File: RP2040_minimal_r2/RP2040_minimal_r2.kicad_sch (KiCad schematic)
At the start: 44 parts, among them J1 SPI0.6, J10 B22, J11 B23, J12 Breakout, J2 SPI0.8, J3 SPI1.13, J4 I2C0, J5 USB, J6 B18, J7 B19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

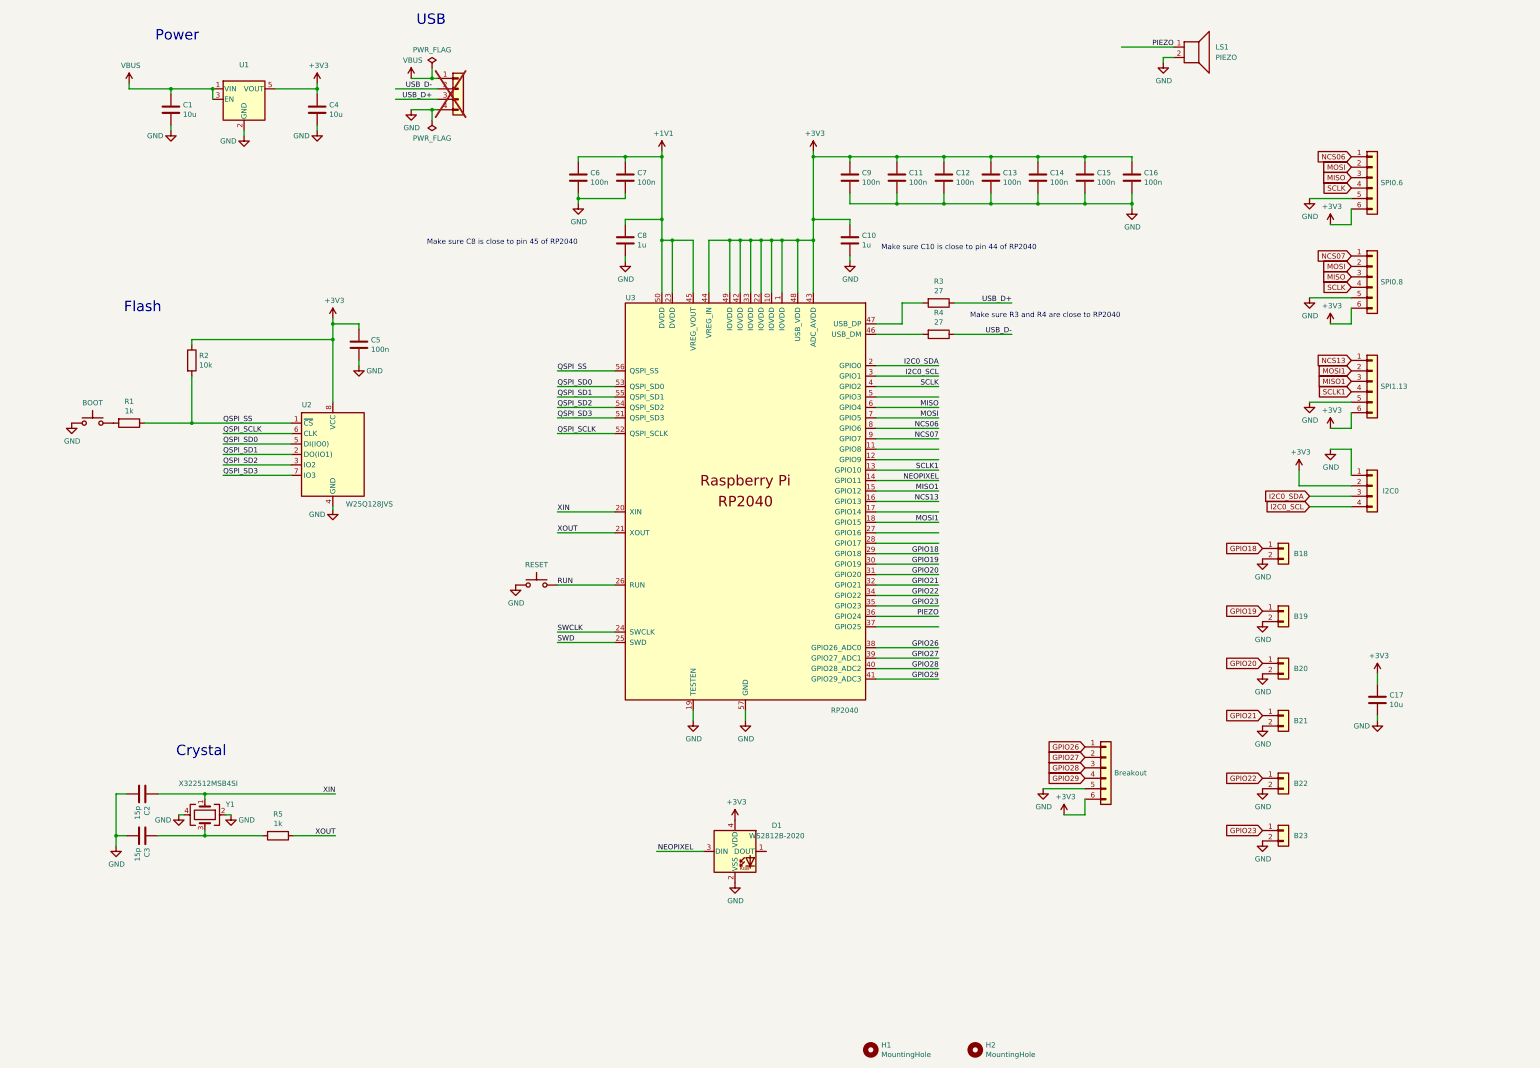
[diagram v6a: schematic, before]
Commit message: Fix incorrect pins used for SPI0. Changed button pins to GPIO 16-21 for slightly cleaner layout. Moved USB header closer to board edge, to allow JST-XH connector to be attached the other way around. Other minor tweaks to top side layout.
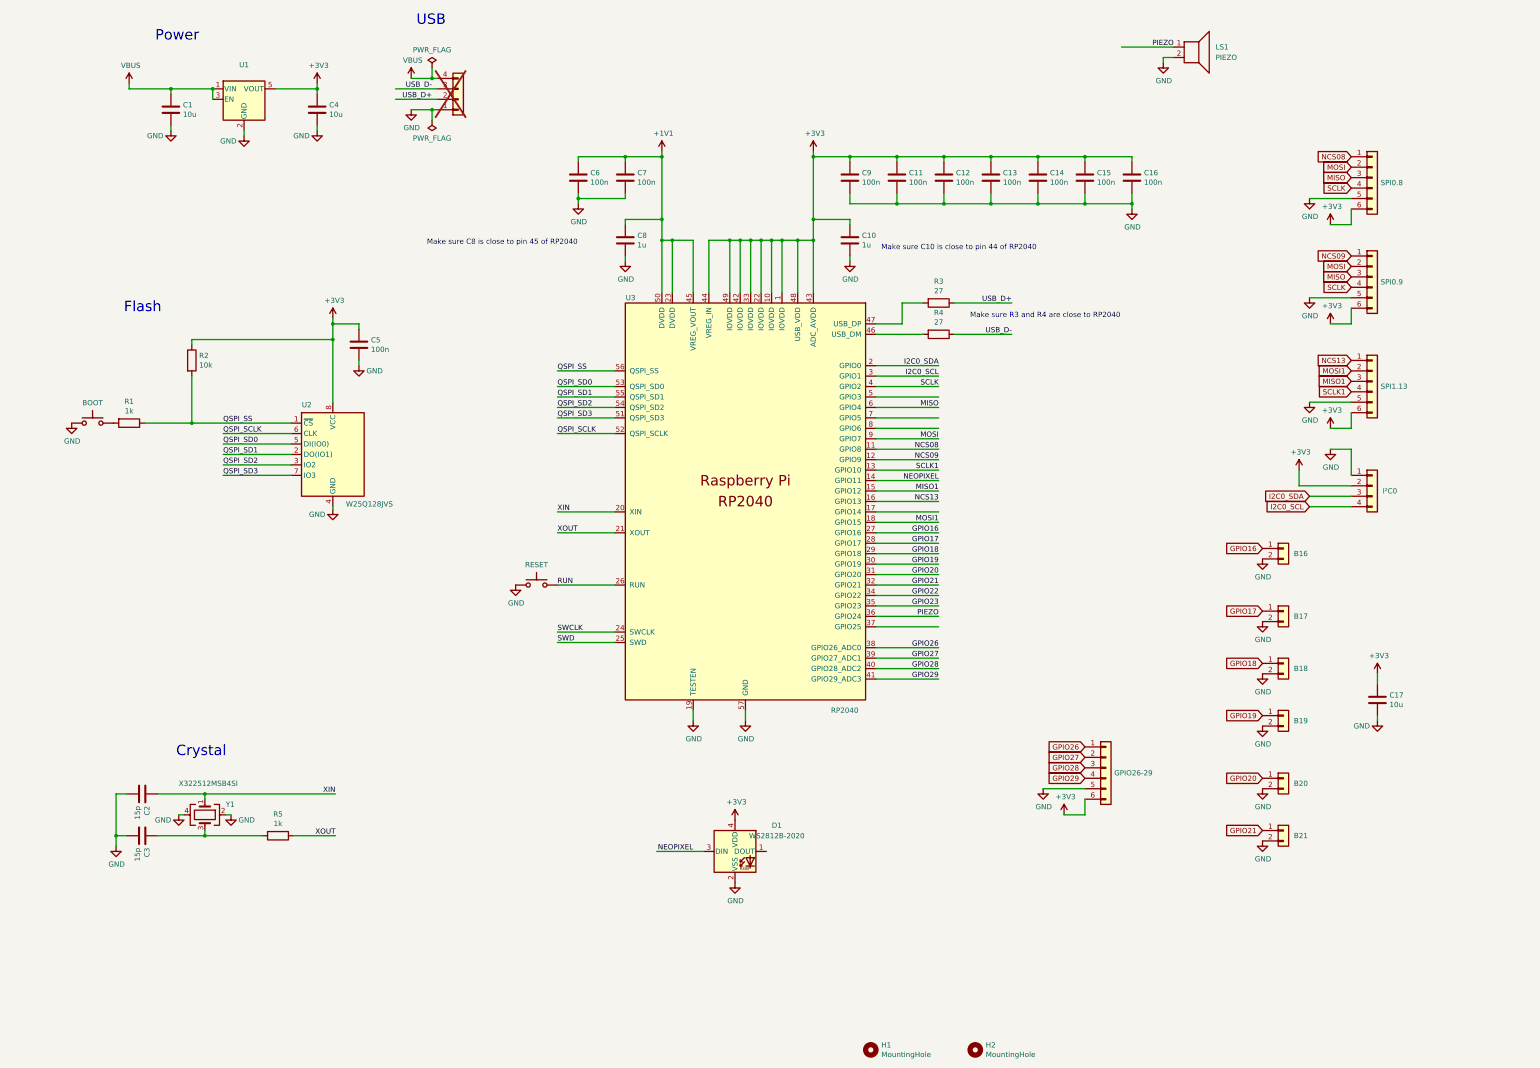
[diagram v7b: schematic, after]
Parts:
- J1: value SPI0.6 -> SPI0.8
- J10: value B22 -> B20
- J11: value B23 -> B21
- J12: value Breakout -> GPIO26-29
- J2: value SPI0.8 -> SPI0.9
- J4: value I2C0 -> I²C0
- J6: value B18 -> B16
- J7: value B19 -> B17
- J8: value B20 -> B18
- J9: value B21 -> B19
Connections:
- net GND: now also J5.1 (Pin_1); no longer J5.4 (Pin_4)
- net GPIO18: now also J8.1 (Pin_1); no longer J6.1 (Pin_1)
- net GPIO19: now also J9.1 (Pin_1); no longer J7.1 (Pin_1)
- net GPIO20: now also J10.1 (Pin_1); no longer J8.1 (Pin_1)
- net GPIO21: now also J11.1 (Pin_1); no longer J9.1 (Pin_1)
- net GPIO22: no longer J10.1 (Pin_1)
- net GPIO23: no longer J11.1 (Pin_1)
- net MOSI: now also U3.9 (GPIO7); no longer U3.7 (GPIO5)
- net USB_D+: now also J5.2 (Pin_2); no longer J5.3 (Pin_3)
- net USB_D-: now also J5.3 (Pin_3); no longer J5.2 (Pin_2)
- net VBUS: now also J5.4 (Pin_4); no longer J5.1 (Pin_1)
- net NCS08: now reaches U3.11 (GPIO8)
- net NCS08: now also J1.1 (Pin_1)
- net NCS09: now reaches U3.12 (GPIO9)
- net NCS09: now also J2.1 (Pin_1)
- net GPIO16: now reaches U3.27 (GPIO16)
- net GPIO16: now also J6.1 (Pin_1)
- net GPIO17: now reaches U3.28 (GPIO17)
- net GPIO17: now also J7.1 (Pin_1)
- net NCS06: no longer names the net of U3.8 (GPIO6)
- net NCS06: no longer J1.1 (Pin_1)
- removed net NCS07: J2.1 (Pin_1), U3.9 (GPIO7)
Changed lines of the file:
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@@
 		)
 	)
-	(label "PIEZO"
-		(at 245.11 172.72 180)
+	(label "MOSI"
+		(at 245.11 129.54 180)
 		(fields_autoplaced yes)
 		(effects
@@
 		)
 	)
-	(label "NEOPIXEL"
-		(at 185.42 229.87 180)
+	(label "PIEZO"
+		(at 245.11 172.72 180)
 		(fields_autoplaced yes)
 		(effects
@@
 		)
 	)
-	(label "NCS06"
-		(at 245.11 127 180)
+	(label "NEOPIXEL"
+		(at 185.42 229.87 180)
 		(fields_autoplaced yes)
 		(effects
@@
 		)
 	)
-	(label "MOSI"
-		(at 245.11 124.46 180)
-		(fields_autoplaced yes)
-		(effects
-			(font
-				(size 1.27 1.27)
-			)
-			(justify right bottom)
-		)
-	)
 	(label "GPIO19"
 		(at 245.11 160.02 180)
@@
 		)
 	)
+	(label "GPIO16"
+		(at 245.11 152.4 180)
+		(fields_autoplaced yes)
+		(effects
+			(font
+				(size 1.27 1.27)
+			)
+			(justify right bottom)
+		)
+	)
 	(label "QSPI_SD0"
 		(at 152.4 116.84 0)
@@
 		)
 	)
+	(label "GPIO17"
+		(at 245.11 154.94 180)
+		(fields_autoplaced yes)
+		(effects
+			(font
+				(size 1.27 1.27)
+			)
+			(justify right bottom)
+		)
+	)
 	(label "QSPI_SD0"
 		(at 71.12 130.81 0)
@@
 		)
 	)
+	(label "NCS09"
+		(at 245.11 134.62 180)
+		(fields_autoplaced yes)
+		(effects
+			(font
+				(size 1.27 1.27)
+			)
+			(justify right bottom)
+		)
+	)
 	(label "GPIO18"
 		(at 245.11 157.48 180)
@@
 		)
 	)
-	(label "NCS07"
-		(at 245.11 129.54 180)
+	(label "NCS08"
+		(at 245.11 132.08 180)
 		(fields_autoplaced yes)
 		(effects
@@
 		)
 	)
-	(global_label "GPIO20"
+	(global_label "GPIO18"
 		(shape input)
 		(at 323.85 184.15 180)
@@
 		)
 	)
-	(global_label "NCS07"
+	(global_label "NCS09"
 		(shape input)
 		(at 345.44 85.09 180)
@@
 		)
 	)
-	(global_label "GPIO18"
+	(global_label "GPIO16"
 		(shape input)
 		(at 323.85 156.21 180)
@@
 		)
 	)
-	(global_label "GPIO22"
+	(global_label "GPIO20"
 		(shape input)
 		(at 323.85 212.09 180)
@@
 		)
 	)
-	(global_label "NCS06"
+	(global_label "NCS08"
 		(shape input)
 		(at 345.44 60.96 180)
@@
 		)
 	)
-	(global_label "GPIO23"
+	(global_label "GPIO21"
 		(shape input)
 		(at 323.85 224.79 180)
@@
 		)
 	)
-	(global_label "GPIO21"
+	(global_label "GPIO19"
 		(shape input)
 		(at 323.85 196.85 180)
@@
 		)
 	)
-	(global_label "GPIO19"
+	(global_label "GPIO17"
 		(shape input)
 		(at 323.85 171.45 180)
@@
 	)
 	(symbol
+		(lib_id "Connector_Generic:Conn_01x04")
+		(at 128.27 46.99 0)
+		(mirror x)
+		(unit 1)
+		(exclude_from_sim no)
+		(in_bom yes)
+		(on_board yes)
+		(dnp yes)
+		(property "Reference" "J5"
+			(at 130.302 46.7868 0)
+			(effects
+				(font
+					(size 1.27 1.27)
+				)
+				(justify left)
+				(hide yes)
+			)
+		)
+		(property "Value" "USB"
+			(at 130.302 44.4754 0)
+			(effects
+				(font
+					(size 1.27 1.27)
+				)
+				(justify left)
+				(hide yes)
+			)
+		)
+		(property "Footprint" "Connector_PinHeader_2.54mm:PinHeader_1x04_P2.54mm_Vertical"
+			(at 128.27 46.99 0)
+			(effects
+				(font
+					(size 1.27 1.27)
+				)
+				(hide yes)
+			)
+		)
+		(property "Datasheet" "~"
+			(at 128.27 46.99 0)
+			(effects
+				(font
+					(size 1.27 1.27)
+				)
+				(hide yes)
+			)
+		)
+		(property "Description" ""
+			(at 128.27 46.99 0)
+			(effects
+				(font
+					(size 1.27 1.27)
+				)
+				(hide yes)
+			)
+		)
+		(property "LCSC" ""
+			(at 128.27 46.99 0)
+			(effects
+				(font
+					(size 1.27 1.27)
+				)
+				(hide yes)
+			)
+		)
+		(pin "1"
+		)
+		(pin "2"
+		)
+		(pin "3"
+		)
+		(pin "4"
+		)
+		(instances
+			(project "RP2040_minimal_r2"
+				(path "/8c0b3d8b-46d3-4173-ab1e-a61765f77d61"
+					(reference "J5")
+					(unit 1)
+				)
+			)
+		)
+	)
+	(symbol
 		(lib_id "PMW3360-rescue:GND-power")
 		(at 335.28 95.25 0)
@@
 			)
 		)
-		(property "Value" "B20"
+		(property "Value" "B18"
 			(at 331.47 185.4199 0)
 			(effects
@@
 			)
 		)
-		(property "Value" "SPI0.8"
+		(property "Value" "SPI0.9"
 			(at 352.552 91.4146 0)
 			(effects
@@
 	)
 	(symbol
-		(lib_id "Connector_Generic:Conn_01x04")
-		(at 128.27 44.45 0)
-		(unit 1)
-		(exclude_from_sim no)
-		(in_bom yes)
-		(on_board yes)
-		(dnp yes)
-		(property "Reference" "J5"
-			(at 130.302 44.6532 0)
-			(effects
-				(font
-					(size 1.27 1.27)
-				)
-				(justify left)
-				(hide yes)
-			)
-		)
-		(property "Value" "USB"
-			(at 130.302 46.9646 0)
-			(effects
-				(font
-					(size 1.27 1.27)
-				)
-				(justify left)
-				(hide yes)
-			)
-		)
-		(property "Footprint" "Connector_PinHeader_2.54mm:PinHeader_1x04_P2.54mm_Vertical"
-			(at 128.27 44.45 0)
-			(effects
-				(font
-					(size 1.27 1.27)
-				)
-				(hide yes)
-			)
-		)
-		(property "Datasheet" "~"
-			(at 128.27 44.45 0)
-			(effects
-				(font
-					(size 1.27 1.27)
-				)
-				(hide yes)
-			)
-		)
-		(property "Description" ""
-			(at 128.27 44.45 0)
-			(effects
-				(font
-					(size 1.27 1.27)
-				)
-				(hide yes)
-			)
-		)
-		(property "LCSC" ""
-			(at 128.27 44.45 0)
-			(effects
-				(font
-					(size 1.27 1.27)
-				)
-				(hide yes)
-			)
-		)
-		(pin "1"
-		)
-		(pin "2"
-		)
-		(pin "3"
-		)
-		(pin "4"
-		)
-		(instances
-			(project "RP2040_minimal_r2"
-				(path "/8c0b3d8b-46d3-4173-ab1e-a61765f77d61"
-					(reference "J5")
-					(unit 1)
-				)
-			)
-		)
-	)
-	(symbol
 		(lib_id "PMW3360-rescue:+3V3-power")
 		(at 340.36 77.47 0)
@@
 			)
 		)
-		(property "Value" "Breakout"
+		(property "Value" "GPIO26-29"
 			(at 287.782 210.7946 0)
 			(effects
@@
 			)
 		)
-		(property "Value" "I2C0"
+		(property "Value" "I²C0"
 			(at 353.06 142.2399 0)
 			(effects
@@
 			)
 		)
-		(property "Value" "B21"
+		(property "Value" "B19"
 			(at 331.47 198.1199 0)
 			(effects
@@
 			)
 		)
-		(property "Value" "B19"
+		(property "Value" "B17"
 			(at 331.47 172.7199 0)
 			(effects
@@
 			)
 		)
-		(property "Value" "B22"
+		(property "Value" "B20"
 			(at 331.47 213.3599 0)
 			(effects
@@
 			)
 		)
-		(property "Value" "SPI0.6"
+		(property "Value" "SPI0.8"
 			(at 352.552 67.2846 0)
 			(effects
@@
 			)
 		)
-		(property "Value" "B23"
+		(property "Value" "B21"
 			(at 331.47 226.0599 0)
 			(effects
@@
 			)
 		)
-		(property "Value" "B18"
+		(property "Value" "B16"
 			(at 331.47 157.4799 0)
 			(effects
